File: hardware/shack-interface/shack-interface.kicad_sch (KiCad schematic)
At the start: 13 parts, among them J1 RJ45 LINK, J10 R3 LED, J11 R1 mini-DIN, J12 R2 mini-DIN, J13 R3 mini-DIN, J14 USB4105-GF-A, J2 KILL switch, J3 13.8 V IN, J6 Front panel, J7 KILL state, J8 R1 LED, J9 R2 LED

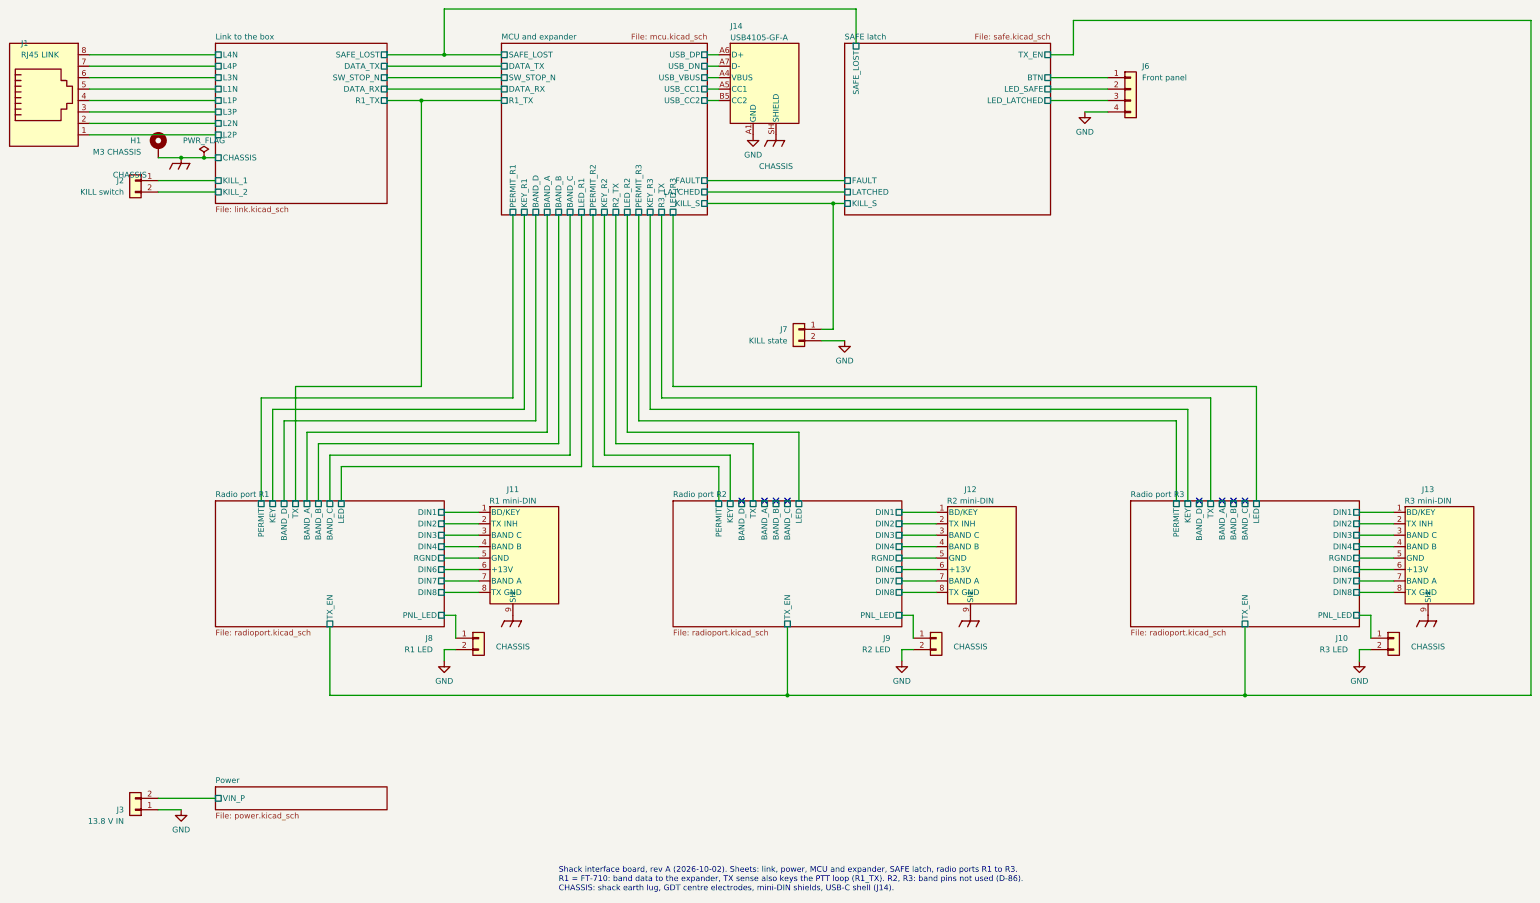
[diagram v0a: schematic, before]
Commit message: Shack interface: end plates, schematic and PCB update; design log
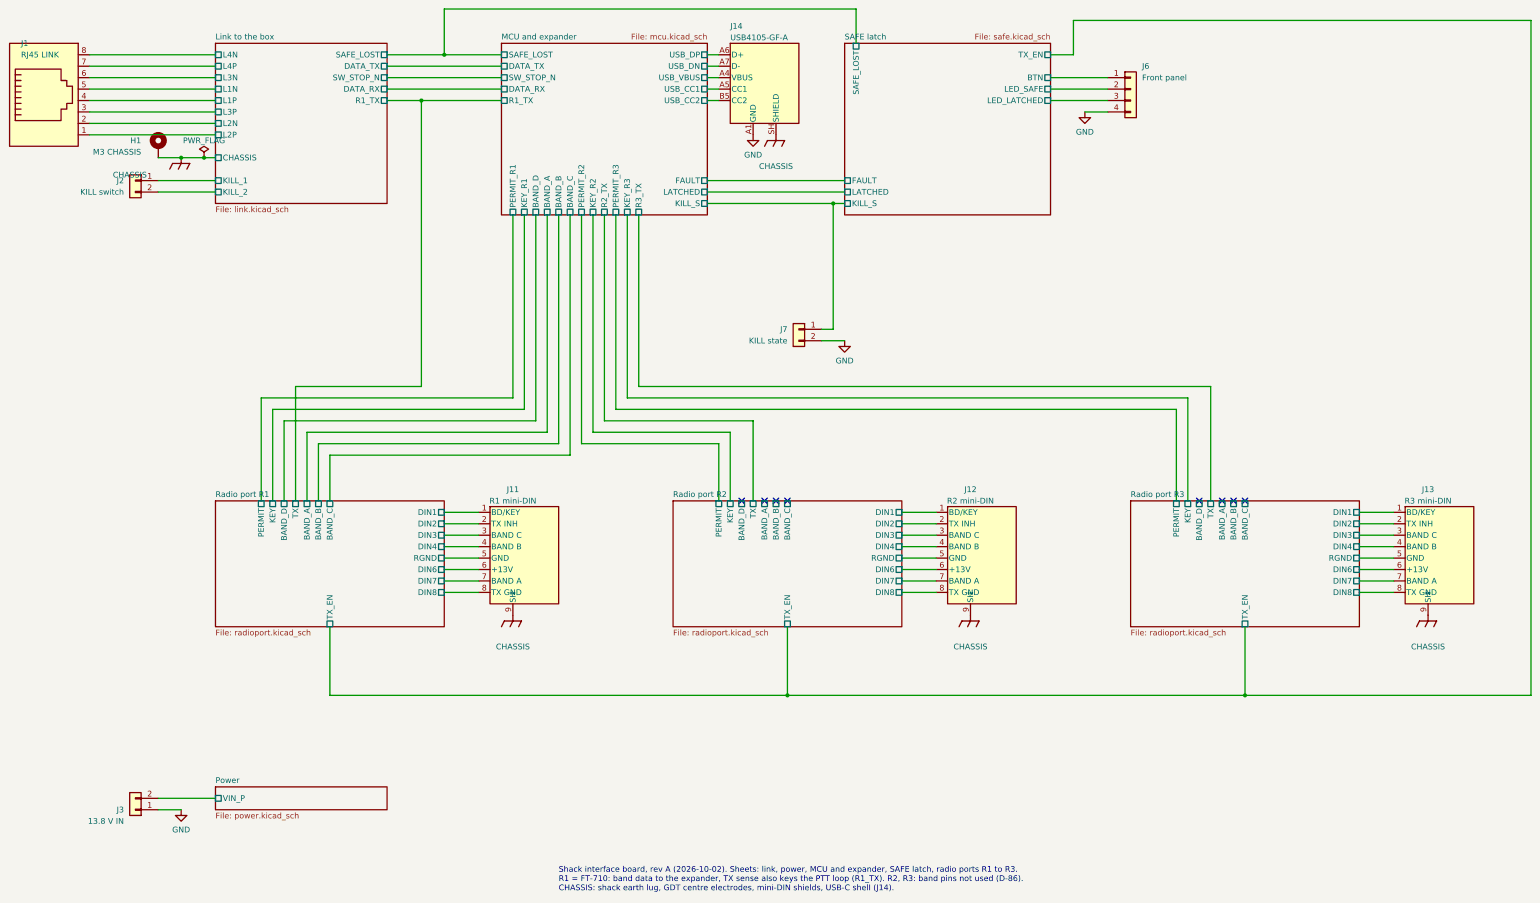
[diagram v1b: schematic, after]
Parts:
- removed J10: R3 LED, Connector_JST:JST_XH_B2B-XH-A_1x02_P2.50mm_Vertical, symbol Connector_Generic:Conn_01x02
- removed J8: R1 LED, Connector_JST:JST_XH_B2B-XH-A_1x02_P2.50mm_Vertical, symbol Connector_Generic:Conn_01x02
- removed J9: R2 LED, Connector_JST:JST_XH_B2B-XH-A_1x02_P2.50mm_Vertical, symbol Connector_Generic:Conn_01x02
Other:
- sheet MCU and expander ports: added none; removed LED_R1, LED_R2, LED_R3
- sheet Radio port R1 ports: added none; removed LED, PNL_LED
- sheet Radio port R2 ports: added none; removed LED, PNL_LED
- sheet Radio port R3 ports: added none; removed LED, PNL_LED
